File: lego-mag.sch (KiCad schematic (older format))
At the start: 20 parts, among them IC1 4N35, P1 CONN_1, P2 CONN_1, P3 CONN_2, P5 CONN_1, P6 CONN_1, Q1 NPN

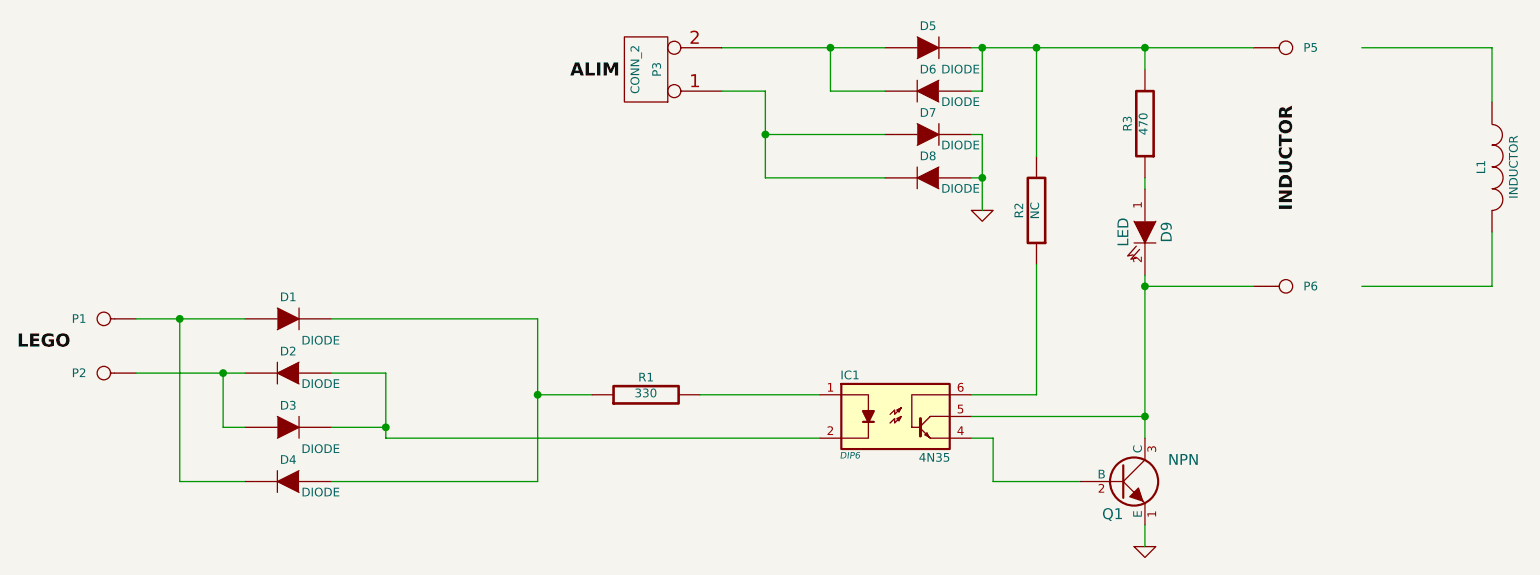
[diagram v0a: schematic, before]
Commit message: Update to v1 with correct diode connection
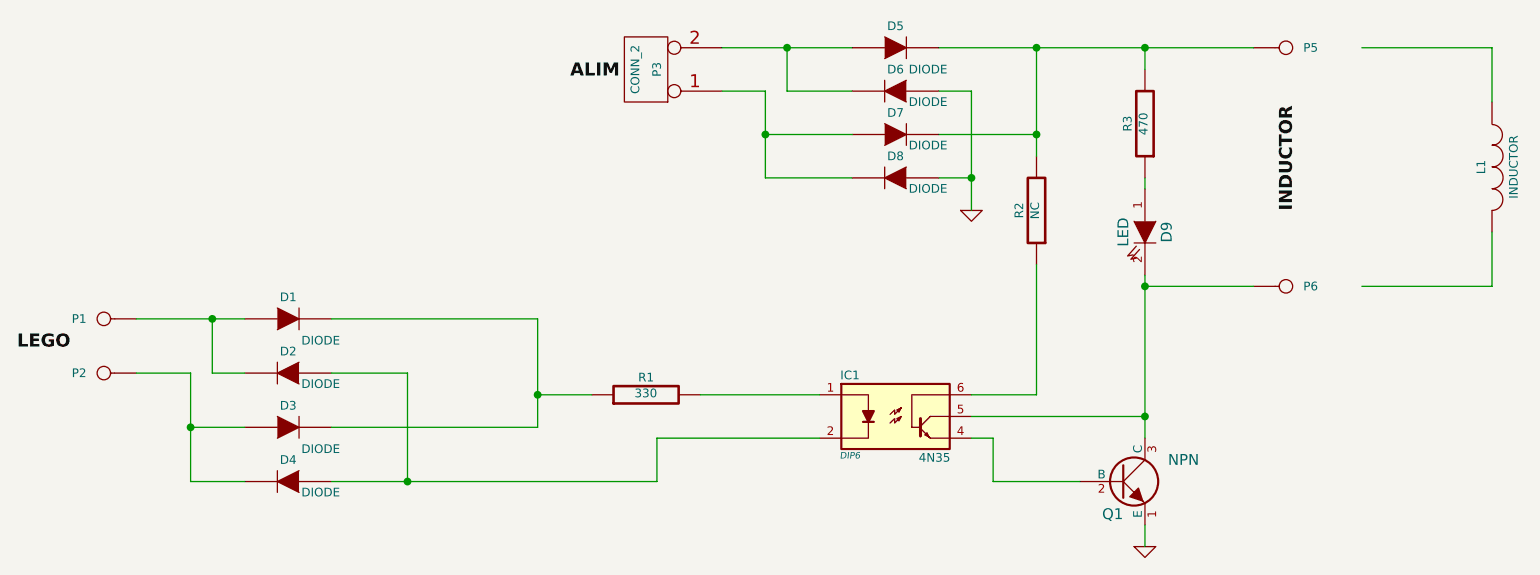
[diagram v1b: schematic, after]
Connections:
- wire segments 44 -> 45
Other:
- moved on the sheet: D5, D6, D7, D8
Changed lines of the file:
@@
 LIBS:contrib
 LIBS:valves
+LIBS:lego-mag-cache
 EELAYER 24 0
 EELAYER END
@@
 	-1   0    0    1
 $EndComp
-Wire Wire Line
-	2500 3950 3000 3950
-Wire Wire Line
-	3400 3950 4350 3950
-Wire Wire Line
-	4350 3950 4350 4700
-Wire Wire Line
-	4350 4300 4600 4300
-Wire Wire Line
-	5100 4300 5650 4300
-Wire Wire Line
-	5650 4500 3650 4500
-Wire Wire Line
-	3650 4500 3650 4200
-Wire Wire Line
-	3650 4200 3400 4200
-Wire Wire Line
-	3400 4450 3650 4450
-Connection ~ 3650 4450
-Wire Wire Line
-	4350 4700 3400 4700
-Connection ~ 4350 4300
-Wire Wire Line
-	2500 4200 3000 4200
-Wire Wire Line
-	2900 4200 2900 4450
-Wire Wire Line
-	2900 4450 3000 4450
-Connection ~ 2900 4200
-Wire Wire Line
-	2700 3950 2700 4700
-Wire Wire Line
-	2700 4700 3000 4700
-Connection ~ 2700 3950
 $Comp
 L DIODE D5
 U 1 1 53D009F6
-P 6150 2700
-F 0 "D5" H 6150 2800 40  0000 C CNN
-F 1 "DIODE" H 6300 2600 40  0000 C CNN
-F 2 "" H 6150 2700 60  0000 C CNN
-F 3 "" H 6150 2700 60  0000 C CNN
-	1    6150 2700
+P 6000 2700
+F 0 "D5" H 6000 2800 40  0000 C CNN
+F 1 "DIODE" H 6150 2600 40  0000 C CNN
+F 2 "" H 6000 2700 60  0000 C CNN
+F 3 "" H 6000 2700 60  0000 C CNN
+	1    6000 2700
 	1    0    0    -1
 $EndComp
@@
 L DIODE D6
 U 1 1 53D00A0D
-P 6150 2900
-F 0 "D6" H 6150 2800 40  0000 C CNN
-F 1 "DIODE" H 6000 2950 40  0000 C CNN
-F 2 "" H 6150 2900 60  0000 C CNN
-F 3 "" H 6150 2900 60  0000 C CNN
-	1    6150 2900
+P 6000 2900
+F 0 "D6" H 6000 2800 40  0000 C CNN
+F 1 "DIODE" H 5850 2950 40  0000 C CNN
+F 2 "" H 6000 2900 60  0000 C CNN
+F 3 "" H 6000 2900 60  0000 C CNN
+	1    6000 2900
 	-1   0    0    1
 $EndComp
@@
 L DIODE D7
 U 1 1 53D00A13
-P 6150 3100
-F 0 "D7" H 6150 3200 40  0000 C CNN
-F 1 "DIODE" H 6300 3050 40  0000 C CNN
-F 2 "" H 6150 3100 60  0000 C CNN
-F 3 "" H 6150 3100 60  0000 C CNN
-	1    6150 3100
+P 6000 3100
+F 0 "D7" H 6000 3200 40  0000 C CNN
+F 1 "DIODE" H 6150 3050 40  0000 C CNN
+F 2 "" H 6000 3100 60  0000 C CNN
+F 3 "" H 6000 3100 60  0000 C CNN
+	1    6000 3100
 	1    0    0    -1
 $EndComp
@@
 L DIODE D8
 U 1 1 53D00A19
-P 6150 3300
-F 0 "D8" H 6150 3200 40  0000 C CNN
-F 1 "DIODE" H 6000 3350 40  0000 C CNN
-F 2 "" H 6150 3300 60  0000 C CNN
-F 3 "" H 6150 3300 60  0000 C CNN
-	1    6150 3300
-	-1   0    0    1
-$EndComp
-Wire Wire Line
-	5200 2700 5950 2700
-Wire Wire Line
-	5200 2900 5400 2900
-Wire Wire Line
-	5400 2900 5400 3300
-Wire Wire Line
-	5400 3300 5950 3300
-Wire Wire Line
-	5950 3100 5400 3100
-Connection ~ 5400 3100
-Wire Wire Line
-	5950 2900 5700 2900
-Wire Wire Line
-	5700 2900 5700 2700
-Connection ~ 5700 2700
-Wire Wire Line
-	6350 2900 6400 2900
-Wire Wire Line
-	6400 2900 6400 2700
-Wire Wire Line
-	6350 3100 6400 3100
-Wire Wire Line
-	6400 3100 6400 3450
-Wire Wire Line
-	6400 3300 6350 3300
-Wire Wire Line
-	6450 4500 6350 4500
+P 6000 3300
+F 0 "D8" H 6000 3200 40  0000 C CNN
+F 1 "DIODE" H 5850 3350 40  0000 C CNN
+F 2 "" H 6000 3300 60  0000 C CNN
+F 3 "" H 6000 3300 60  0000 C CNN
+	1    6000 3300
+	-1   0    0    1
+$EndComp
 $Comp
 L GND #PWR01
 U 1 1 53D00B0C
-P 6400 3450
-F 0 "#PWR01" H 6400 3450 30  0001 C CNN
-F 1 "GND" H 6400 3380 30  0001 C CNN
-F 2 "" H 6400 3450 60  0000 C CNN
-F 3 "" H 6400 3450 60  0000 C CNN
-	1    6400 3450
-	1    0    0    -1
-$EndComp
-Connection ~ 6400 3300
-Connection ~ 6400 2700
+P 6350 3450
+F 0 "#PWR01" H 6350 3450 30  0001 C CNN
+F 1 "GND" H 6350 3380 30  0001 C CNN
+F 2 "" H 6350 3450 60  0000 C CNN
+F 3 "" H 6350 3450 60  0000 C CNN
+	1    6350 3450
+	1    0    0    -1
+$EndComp
 $Comp
 L CONN_1 P5
@@
 	-1   0    0    1
 $EndComp
-Wire Wire Line
-	6650 3200 6650 2700
-Connection ~ 6650 2700
-Wire Wire Line
-	6650 3700 6650 4300
 $Comp
 L R R3
@@
 	1    0    0    -1
 $EndComp
-Wire Wire Line
-	6650 4300 6350 4300
 $Comp
 L NPN Q1
@@
 	1    0    0    -1
 $EndComp
-Wire Wire Line
-	7150 5000 7150 4900
-Wire Wire Line
-	6850 4700 6450 4700
-Wire Wire Line
-	6450 4700 6450 4500
-Wire Wire Line
-	6350 4400 7150 4400
-Wire Wire Line
-	7150 3750 7150 4500
-Wire Wire Line
-	6350 2700 7650 2700
-Wire Wire Line
-	7150 2800 7150 2700
-Connection ~ 7150 2700
-Connection ~ 7150 4400
-Wire Wire Line
-	7150 3350 7150 3300
-Wire Wire Line
-	7650 3800 7150 3800
-Connection ~ 7150 3800
-Wire Wire Line
-	8150 3800 8750 3800
-Wire Wire Line
-	8750 3800 8750 3550
-Wire Wire Line
-	8750 2950 8750 2700
-Wire Wire Line
-	8750 2700 8150 2700
 Text Label 1950 4100 0    60   ~ 12
 LEGO
@@
 	-1   0    0    1
 $EndComp
+Wire Wire Line
+	2500 3950 3000 3950
+Wire Wire Line
+	3400 3950 4350 3950
+Wire Wire Line
+	4350 4300 4600 4300
+Wire Wire Line
+	5100 4300 5650 4300
+Connection ~ 4350 4300
+Wire Wire Line
+	5200 2900 5400 2900
+Wire Wire Line
+	6450 4500 6350 4500
+Wire Wire Line
+	6650 3200 6650 2700
+Connection ~ 6650 2700
+Wire Wire Line
+	6650 3700 6650 4300
+Wire Wire Line
+	6650 4300 6350 4300
+Wire Wire Line
+	7150 5000 7150 4900
+Wire Wire Line
+	6850 4700 6450 4700
+Wire Wire Line
+	6450 4700 6450 4500
+Wire Wire Line
+	6350 4400 7150 4400
+Wire Wire Line
+	7150 3750 7150 4500
+Wire Wire Line
+	7150 2800 7150 2700
+Connection ~ 7150 2700
+Connection ~ 7150 4400
+Wire Wire Line
+	7150 3350 7150 3300
+Wire Wire Line
+	7650 3800 7150 3800
+Connection ~ 7150 3800
+Wire Wire Line
+	8150 3800 8750 3800
+Wire Wire Line
+	8750 3800 8750 3550
+Wire Wire Line
+	8750 2950 8750 2700
+Wire Wire Line
+	8750 2700 8150 2700
+Wire Wire Line
+	4350 3950 4350 4450
+Wire Wire Line
+	2500 4200 2750 4200
+Wire Wire Line
+	2750 4200 2750 4700
+Wire Wire Line
+	2750 4450 3000 4450
+Wire Wire Line
+	4350 4450 3400 4450
+Wire Wire Line
+	5650 4500 4900 4500
+Wire Wire Line
+	4900 4500 4900 4700
+Wire Wire Line
+	4900 4700 3400 4700
+Wire Wire Line
+	2750 4700 3000 4700
+Connection ~ 2750 4450
+Wire Wire Line
+	3750 4700 3750 4200
+Wire Wire Line
+	3750 4200 3400 4200
+Connection ~ 3750 4700
+Wire Wire Line
+	3000 4200 2850 4200
+Wire Wire Line
+	2850 4200 2850 3950
+Connection ~ 2850 3950
+Wire Wire Line
+	6200 2700 7650 2700
+Wire Wire Line
+	5200 2700 5800 2700
+Wire Wire Line
+	5400 2900 5400 3300
+Wire Wire Line
+	5400 3100 5800 3100
+Wire Wire Line
+	6200 3100 6650 3100
+Connection ~ 6650 3100
+Wire Wire Line
+	6350 2900 6350 3450
+Wire Wire Line
+	6350 3300 6200 3300
+Wire Wire Line
+	5400 3300 5800 3300
+Connection ~ 5400 3100
+Wire Wire Line
+	6350 2900 6200 2900
+Connection ~ 6350 3300
+Wire Wire Line
+	5800 2900 5500 2900
+Wire Wire Line
+	5500 2900 5500 2700
+Connection ~ 5500 2700
 $EndSCHEMATC
